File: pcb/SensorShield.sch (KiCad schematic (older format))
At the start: 61 parts, among them U14 ICE40UP5K-SG48ITR, U15 GD25Q32CTIGR-Memory_Flash

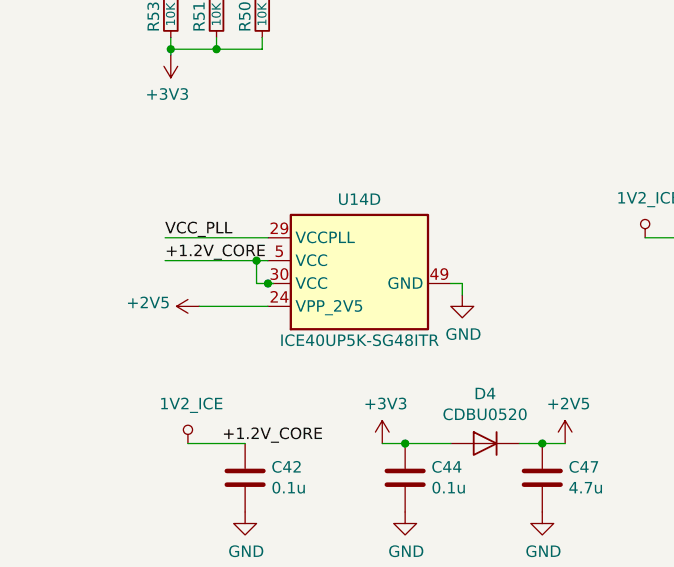
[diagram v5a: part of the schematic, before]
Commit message: Solved connections showed wrong by ERC
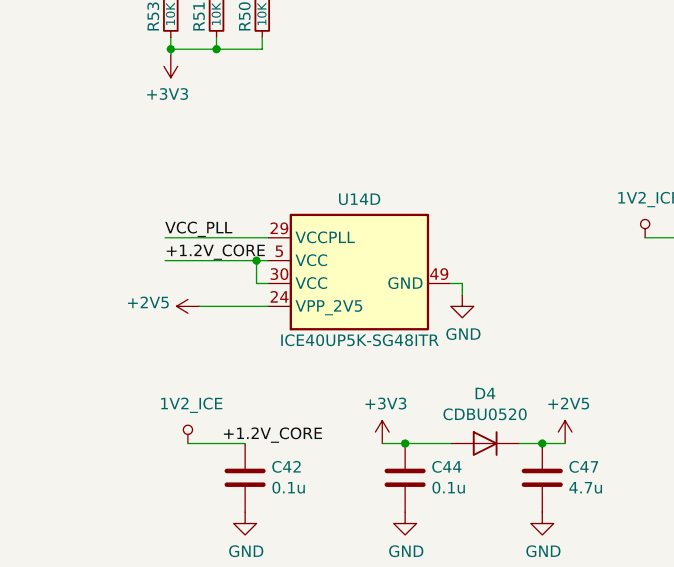
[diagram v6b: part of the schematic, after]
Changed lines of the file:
@@
 EESchema Schematic File Version 4
-LIBS:keep_breathing_ctrl-cache
 EELAYER 30 0
 EELAYER END
@@
 SPI_CLK
 Wire Wire Line
-	1575 5600 1550 5600
-Wire Wire Line
 	1500 5600 1500 5500
-Connection ~ 1550 5600
-Wire Wire Line
-	1550 5600 1500 5600
 Connection ~ 1500 5500
 Wire Wire Line
@@
 Wire Wire Line
 	1325 4525 1325 4575
+Connection ~ 1325 4575
+Wire Wire Line
+	1325 4575 1125 4575
+Wire Wire Line
+	1550 5600 1500 5600
 Wire Bus Line
 	2250 9700 2250 10300
 Wire Bus Line
 	9700 7600 9700 8450
-Connection ~ 1325 4575
-Wire Wire Line
-	1325 4575 1125 4575
 $EndSCHEMATC

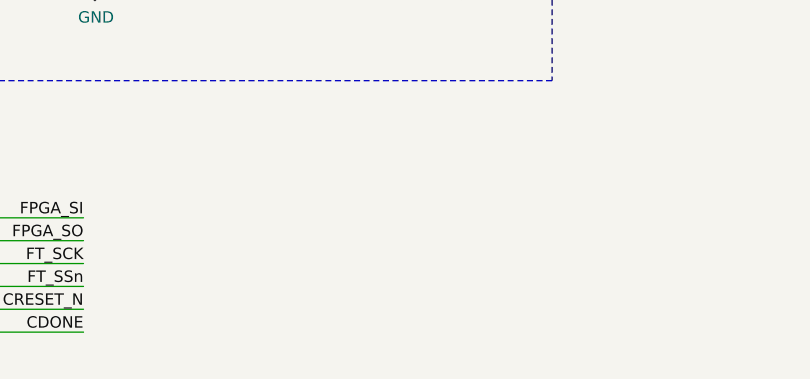
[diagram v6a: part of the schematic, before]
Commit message: Solved connection problem with XCL214B333DR and it was added 3 leds to the board
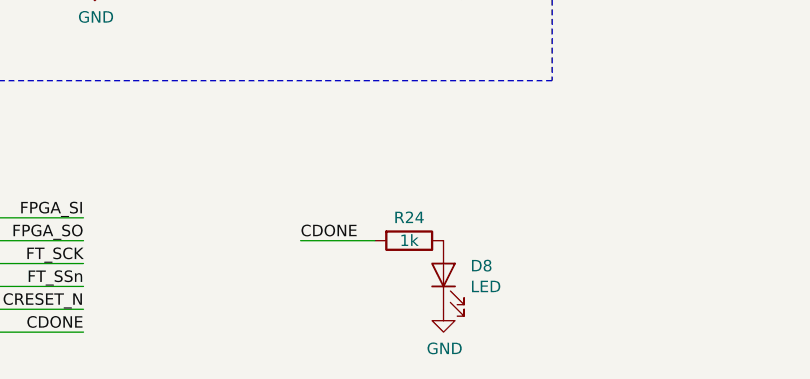
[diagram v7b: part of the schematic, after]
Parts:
- added D8: LED, LED_SMD:LED_0603_1608Metric, symbol Device:LED
- added R24: 1k, Resistor_SMD:R_0402_1005Metric, symbol Device:R
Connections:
- net CDONE: now also R24.2
- net GND: now also D8.1 (K)
- new net: D8.2 (A), R24.1
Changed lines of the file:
@@
 Wire Wire Line
 	1550 5600 1500 5600
+Wire Wire Line
+	4675 10000 4350 10000
+Text Label 4350 10000 0    50   ~ 0
+CDONE
+$Comp
+L Device:R R?
+U 1 1 5EF8349E
+P 4825 10000
+AR Path="/5EA61A2E/5EF8349E" Ref="R?"  Part="1"
+AR Path="/5E9C016D/5EF8349E" Ref="R24"  Part="1"
+F 0 "R24" V 4725 10000 50  0000 C CNN
+F 1 "1k" V 4825 10000 50  0000 C CNN
+F 2 "Resistor_SMD:R_0402_1005Metric" V 4755 10000 50  0001 C CNN
+F 3 "~" H 4825 10000 50  0001 C CNN
+F 4 "" V 4825 10000 50  0001 C CNN "DigiKey"
+	1    4825 10000
+	0    1    1    0
+$EndComp
+$Comp
+L Device:LED D?
+U 1 1 5EF834A5
+P 4975 10150
+AR Path="/5EA61A2E/5EF834A5" Ref="D?"  Part="1"
+AR Path="/5E9C016D/5EF834A5" Ref="D8"  Part="1"
+F 0 "D8" V 5014 10032 50  0000 R CNN
+F 1 "LED" V 4923 10032 50  0000 R CNN
+F 2 "LED_SMD:LED_0603_1608Metric" H 4975 10150 50  0001 C CNN
+F 3 "~" H 4975 10150 50  0001 C CNN
+F 4 "SML-D12U1WT86CT-ND" V 4975 10150 50  0001 C CNN "Field4"
+	1    4975 10150
+	0    -1   -1   0
+$EndComp
+$Comp
+L power:GND #PWR?
+U 1 1 5EF834B1
+P 4975 10300
+AR Path="/5EA61A2E/5EF834B1" Ref="#PWR?"  Part="1"
+AR Path="/5E9C016D/5EF834B1" Ref="#PWR09"  Part="1"
+F 0 "#PWR09" H 4975 10050 50  0001 C CNN
+F 1 "GND" H 4980 10127 50  0000 C CNN
+F 2 "" H 4975 10300 50  0001 C CNN
+F 3 "" H 4975 10300 50  0001 C CNN
+	1    4975 10300
+	1    0    0    -1
+$EndComp
 Wire Bus Line
 	2250 9700 2250 10300

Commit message: Added digiKey part number for some components
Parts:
- C42, C43, C44, C45, C48, C49, C52, C54, C56, C58, C60, C61, C64, C65, C68, C69: DigiKey (none) -> 1276-1442-1-ND
- C46, C47, C50, C51, C53: DigiKey (none) -> 1276-1056-1-ND
- C55, C57, C59, C62, C63, C66, C67, C70, C71: DigiKey (none) -> 1276-1443-1-ND
- D4: DigiKey (none) -> 641-1332-1-ND
- G0, G1, G2, G3, G4, G5, G6, G7, G8: DigiKey (none) -> S5674-ND
- R24: DigiKey (none) -> P1.0KJCT-ND
- R29, R30, R31, R33, R34, R5, R50, R51, R53: DigiKey (none) -> P10KJDKR-ND
- R32: DigiKey (none) -> P100LCT-ND
- S0, S1, S2, S3, S4, S5, S6, S7, S8: DigiKey (none) -> S5677-ND
